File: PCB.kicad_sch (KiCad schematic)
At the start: 35 parts, among them J1 USB_C_Receptacle_USB2.0, J2 JST - 1.00mm 4 Pin, SW72 SW_Push, SW73 SW_Push, U1 RP2040, U3 USBLC6-2SC6, U4 3.3V Fixed Regulator, U5 ZD25D40CNJGR, Y1 12MHz Crystal 3225

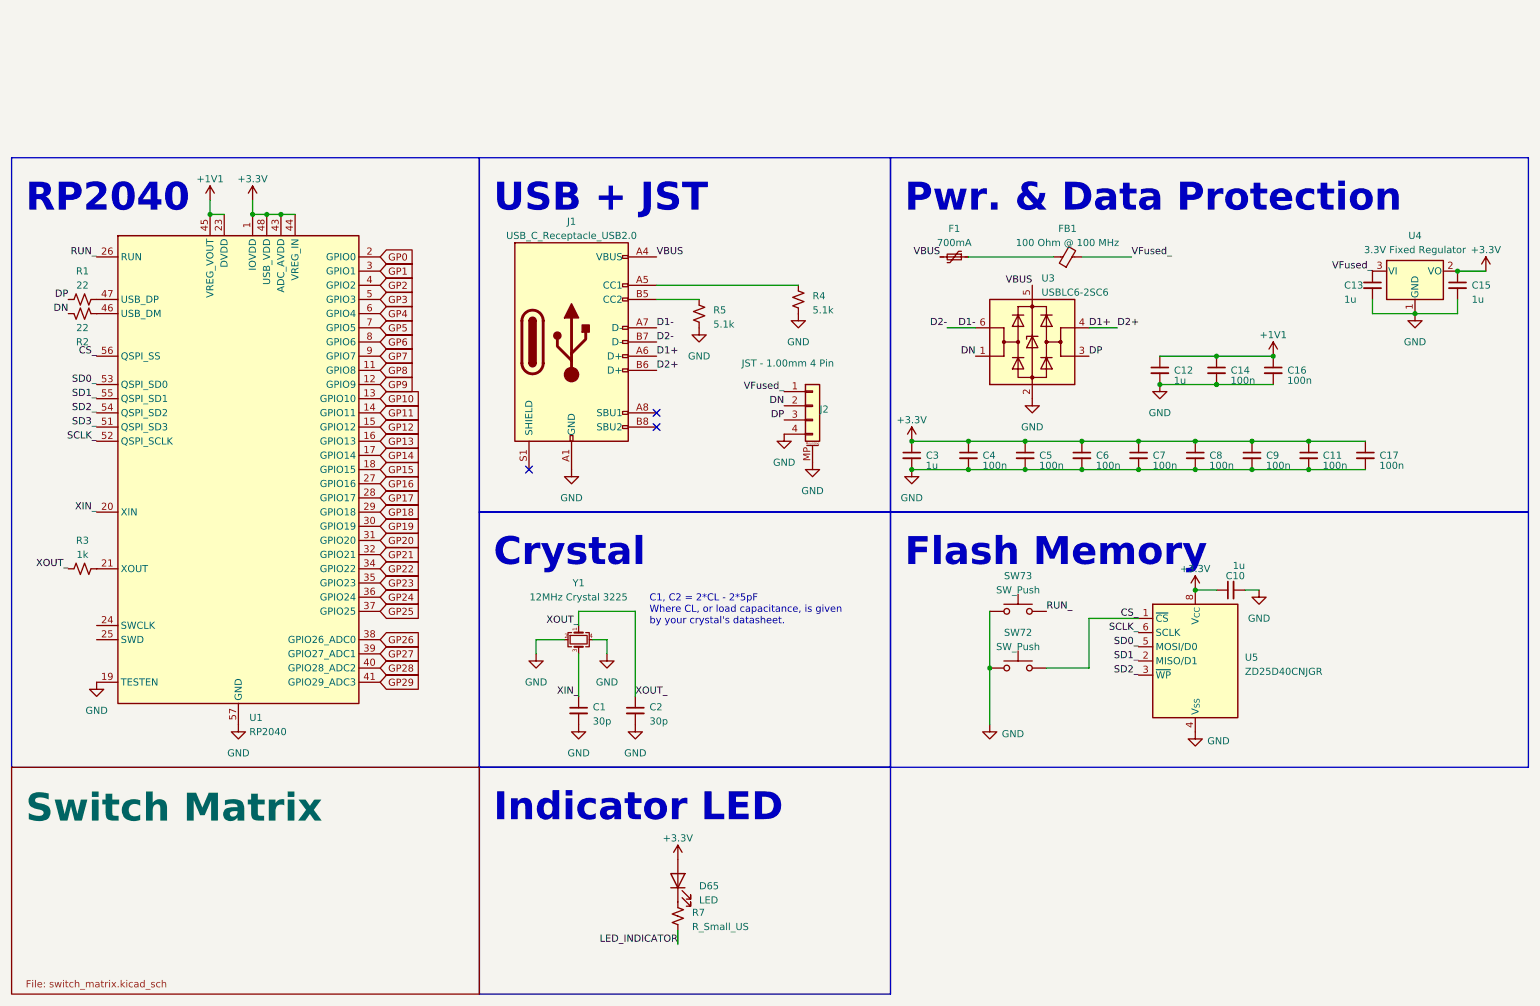
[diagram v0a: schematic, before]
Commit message: update to kicad 8
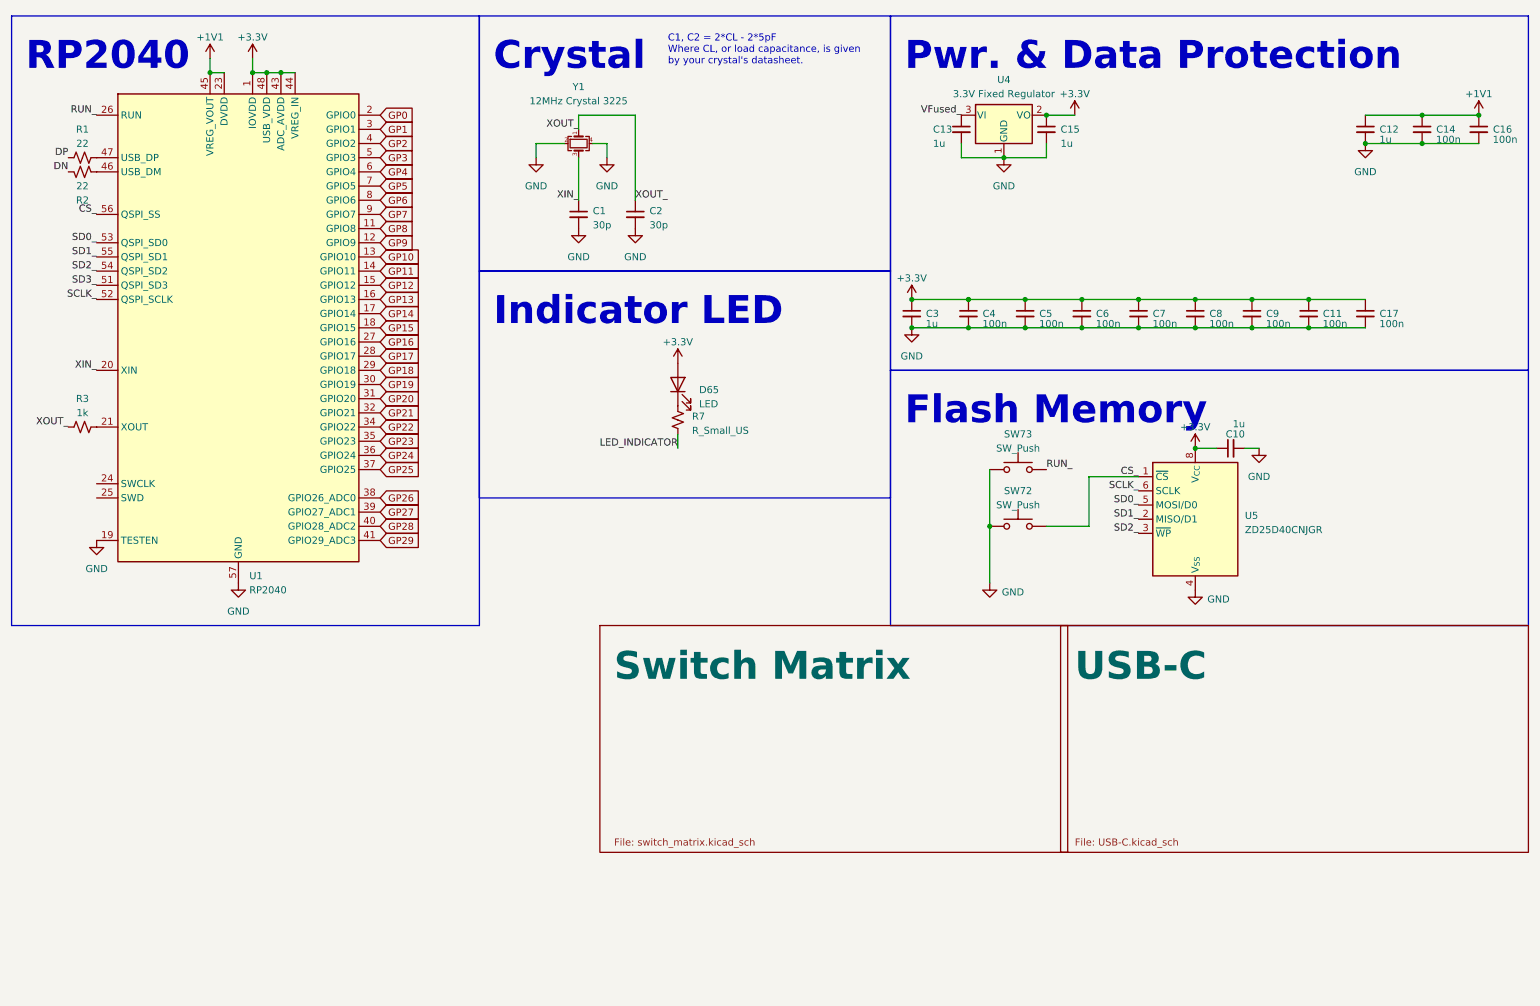
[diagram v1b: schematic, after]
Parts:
- removed F1: 700mA, Fuse:Fuse_0402_1005Metric, symbol Device:Polyfuse_Small
- removed FB1: 100 Ohm @ 100 MHz, Inductor_SMD:L_0402_1005Metric, symbol Device:FerriteBead_Small
- removed J1: USB_C_Receptacle_USB2.0, Connector_USB:USB_C_Receptacle_GCT_USB4085, symbol Connector:USB_C_Receptacle_USB2.0
- removed J2: JST - 1.00mm 4 Pin, Connector_JST:JST_SH_SM04B-SRSS-TB_1x04-1MP_P1.00mm_Horizontal, symbol Connector_Generic_MountingPin:Conn_01x04_MountingPin
- removed R4, R5: 5.1k, Resistor_SMD:R_0402_1005Metric, symbol Device:R_Small_US
- removed U3: USBLC6-2SC6, Package_TO_SOT_SMD:SOT-23-6, symbol Power_Protection:USBLC6-2SC6
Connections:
- no-connect marks 3 -> 0
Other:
- added sheet USB-C (USB-C.kicad_sch)
- note removed: "USB + JST"
- moved on the sheet: C1, C10, C11, C12, C13, C14, C15, C16, C17, C2, C3, C4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

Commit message: keyboard switch comletion
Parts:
- renumbered C1 to C101, C2 to C102, C3 to C103, C13 to C104, C4 to C105, C5 to C106, C15 to C107, C6 to C108, C7 to C109, C8 to C110, C10 to C111, C9 to C112, C11 to C113, C12 to C114, C17 to C115, C14 to C116, C16 to C117, D65 to D101, R1 to R101, R2 to R102, R3 to R103, R7 to R104, SW73 to SW101, SW72 to SW102, U1 to U101, U4 to U102, U5 to U103, Y1 to Y101

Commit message: push de modification
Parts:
- removed C115: 100n, Capacitor_SMD:C_0402_1005Metric, symbol Device:C_Small
- removed SW101, SW102: SW_Push, Button_Switch_SMD:SW_SPST_SKQG_WithoutStem, symbol Switch:SW_Push
- removed U102: 3.3V Fixed Regulator, Package_TO_SOT_SMD:TSOT-23, symbol Regulator_Linear:AP2127N3-1.2
- removed U103: ZD25D40CNJGR, USON8:USON-8_1.5x1.5mm_P0.45mm, symbol Flash_NOR_SPI:ZD25D40CNJGR
- added C17: 2µ2F, Capacitor_SMD:C_0805_2012Metric, symbol Device:C_Small
- added D2: GREEN, Diode_SMD:D_0805_2012Metric, symbol Device:LED
- added R5: 330, Resistor_SMD:R_0603_1608Metric, symbol Device:R_Small_US
- added SW1: SW_CHIP_EN, Button_Switch_SMD:SW_DIP_SPSTx01_Slide_6.7x4.1mm_W6.73mm_P2.54mm_LowProfile_JPin, symbol Switch:SW_Push
- added SW2: SW_BOOT, Button_Switch_SMD:SW_DIP_SPSTx01_Slide_6.7x4.1mm_W6.73mm_P2.54mm_LowProfile_JPin, symbol Switch:SW_Push
- added U2: AP7361C-33E, Package_TO_SOT_SMD:SOT-223-3_TabPin2, symbol Regulator_Linear:AP7361C-33E
- added U3: W25Q16JVSSIQ, Package_SO:SOIC-8_5.23x5.23mm_P1.27mm, symbol Memory_Flash:W25Q16JVSS
- C1: renamed from C101; value 30p -> 6pF
- C10: renamed from C107; value 1u -> 4.7µF; footprint Capacitor_SMD:C_0402_1005Metric -> Capacitor_SMD:C_0805_2012Metric
- C11: renamed from C108; value 100n -> 100nF
- C12: renamed from C109; value 100n -> 100nF
- C13: renamed from C110; value 100n -> 100nF
- C14: renamed from C112; value 100n -> 100nF
- C15: renamed from C113; value 100n -> 100nF
- C16: renamed from C111; value 1u -> 100nF
- C2: renamed from C102; value 30p -> 6pF
- C3: renamed from C114; value 1u -> 2µ2F; footprint Capacitor_SMD:C_0402_1005Metric -> Capacitor_SMD:C_0805_2012Metric
- C4: renamed from C103; value 1u -> 2µ2F; footprint Capacitor_SMD:C_0402_1005Metric -> Capacitor_SMD:C_0805_2012Metric
- C5: renamed from C104; value 1u -> 4.7µF; footprint Capacitor_SMD:C_0402_1005Metric -> Capacitor_SMD:C_0805_2012Metric
- C6: renamed from C116; value 100n -> 100nF
- C7: renamed from C105; value 100n -> 2µ2F; footprint Capacitor_SMD:C_0402_1005Metric -> Capacitor_SMD:C_0805_2012Metric
- C8: renamed from C117; value 100n -> 100nF
- C9: renamed from C106; value 100n -> 100nF
- D1: renamed from D101; value LED -> RED; footprint marbastlib-mx:LED_MX_3mm -> Diode_SMD:D_0805_2012Metric
- R1: renamed from R101; value 22 -> 27; footprint Resistor_SMD:R_0402_1005Metric -> Resistor_SMD:R_0603_1608Metric
- R2: renamed from R102; value 22 -> 27; footprint Resistor_SMD:R_0402_1005Metric -> Resistor_SMD:R_0603_1608Metric
- R3: renamed from R103; footprint Resistor_SMD:R_0402_1005Metric -> Resistor_SMD:R_0603_1608Metric
- R4: renamed from R104; value R_Small_US -> 330; footprint Resistor_SMD:R_0402_1005Metric -> Resistor_SMD:R_0603_1608Metric
- Y1: renamed from Y101; value 12MHz Crystal 3225 -> STDCRG1-12M
- renumbered U101 to U1
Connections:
- net LED_INDICATOR is gone; now on net GP25: R4.2
- net +3.3V: now also C17.1, D2.2 (A), U2.3 (VO), U3.8 (VCC)
- net CS_: now also SW2.2, U3.1 (~{CS})
- net GND: now also C17.2, R5.2, SW1.1, SW2.1, U2.2 (GND), U3.4 (GND)
- net RUN_: now also SW1.2
- net SCLK_: now also U3.6 (CLK)
- net SD0_: now also U3.5 (DI(IO0))
- net SD1_: now also U3.2 (DO(IO1))
- net SD2_: now also U3.3 (IO2)
- net SD3_: now also U3.7 (IO3)
- net DrP: now reaches R1.2, U1.47 (USB_DP)
- net DrN: now reaches R2.1, U1.46 (USB_DM)
- net VFused_ renamed V_Fused
- net V_Fused: now also U2.1 (VI)
- new net: D2.1 (K), R5.1
- no-connect marks 0 -> 3
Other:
- note added: "Flash memory"
- note added: "Pico"
- note added: "Pwr."
- note removed: "Pwr. & Data Protection"
- moved on the sheet: C10, C16, C3, C5, C6, C8, D1, R1, R2, R4
